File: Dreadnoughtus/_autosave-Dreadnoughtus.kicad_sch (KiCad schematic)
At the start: 403 parts

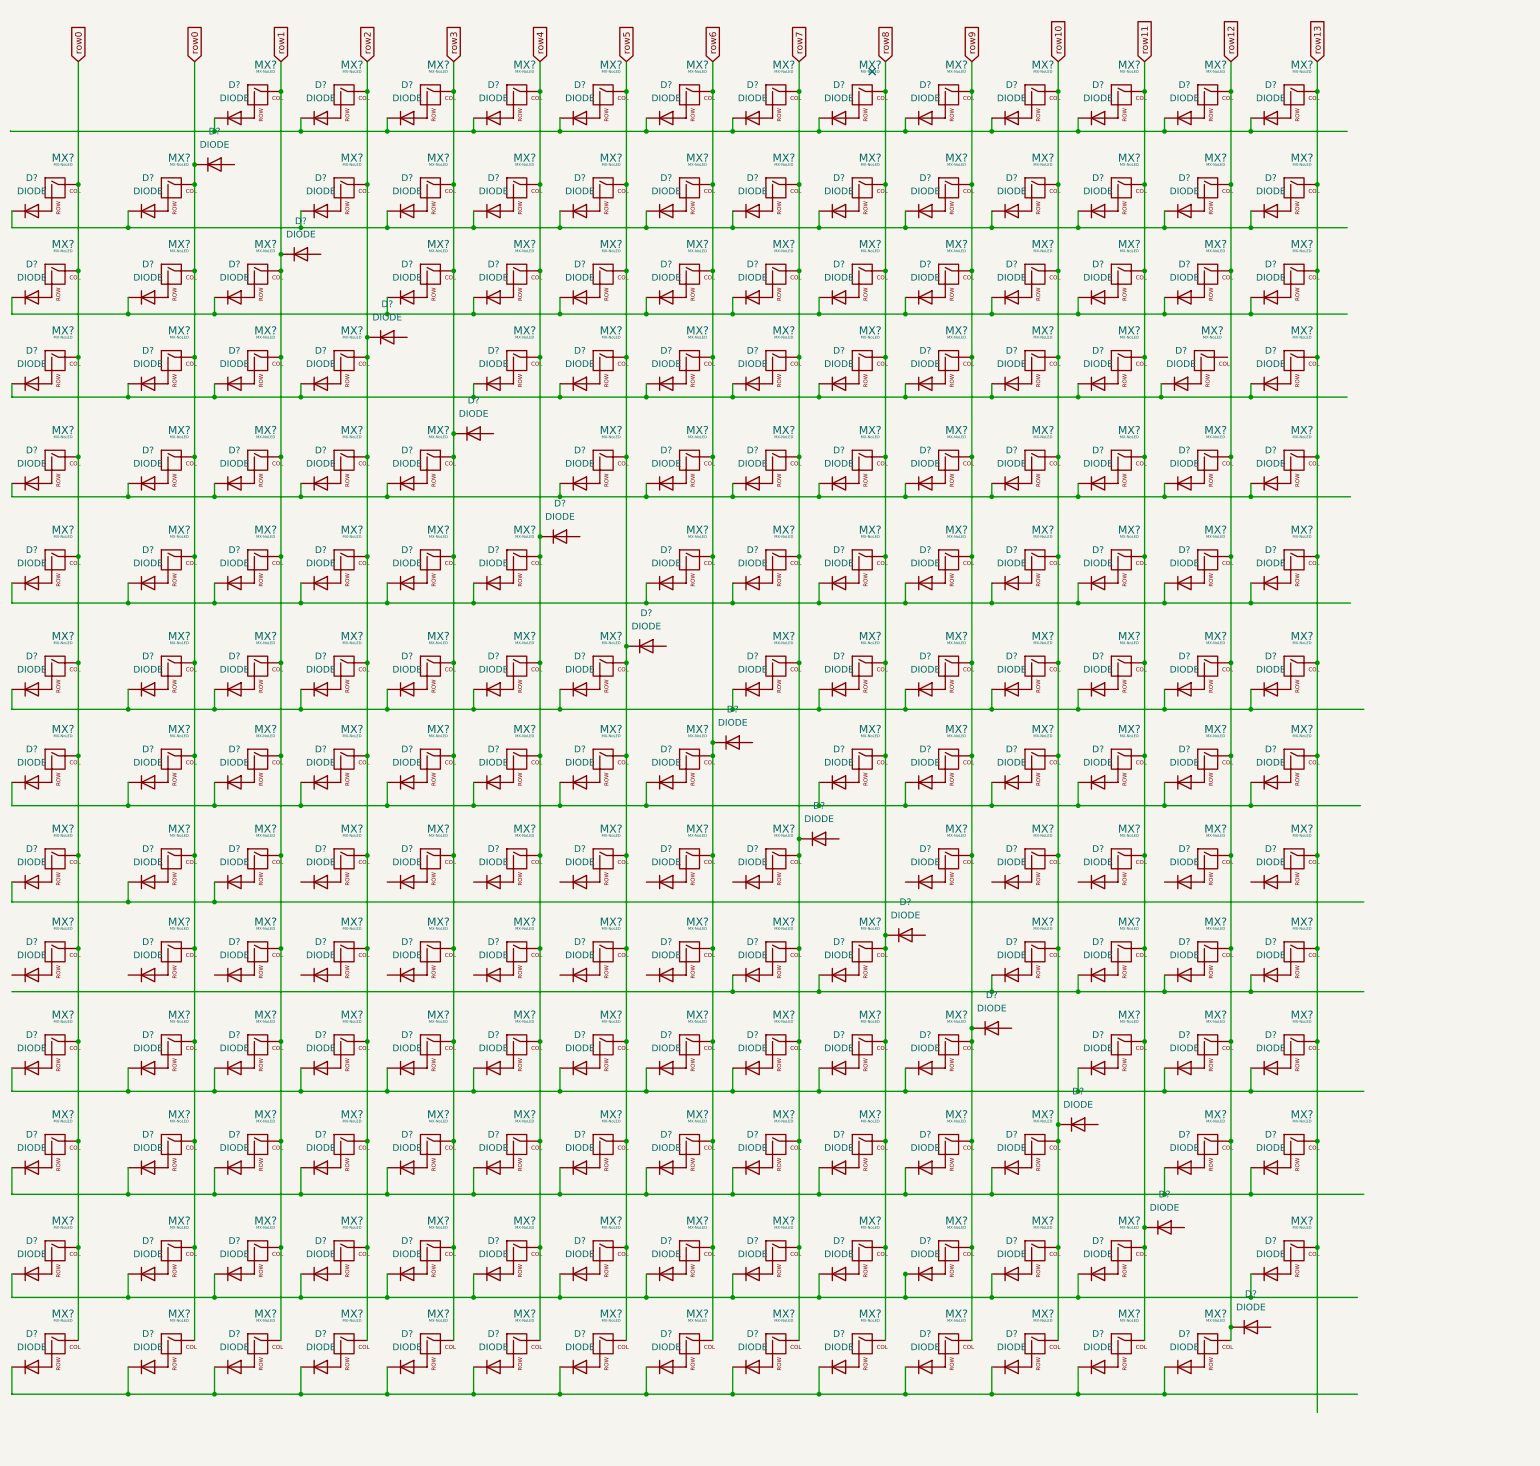
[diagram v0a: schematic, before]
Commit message: added keebio components
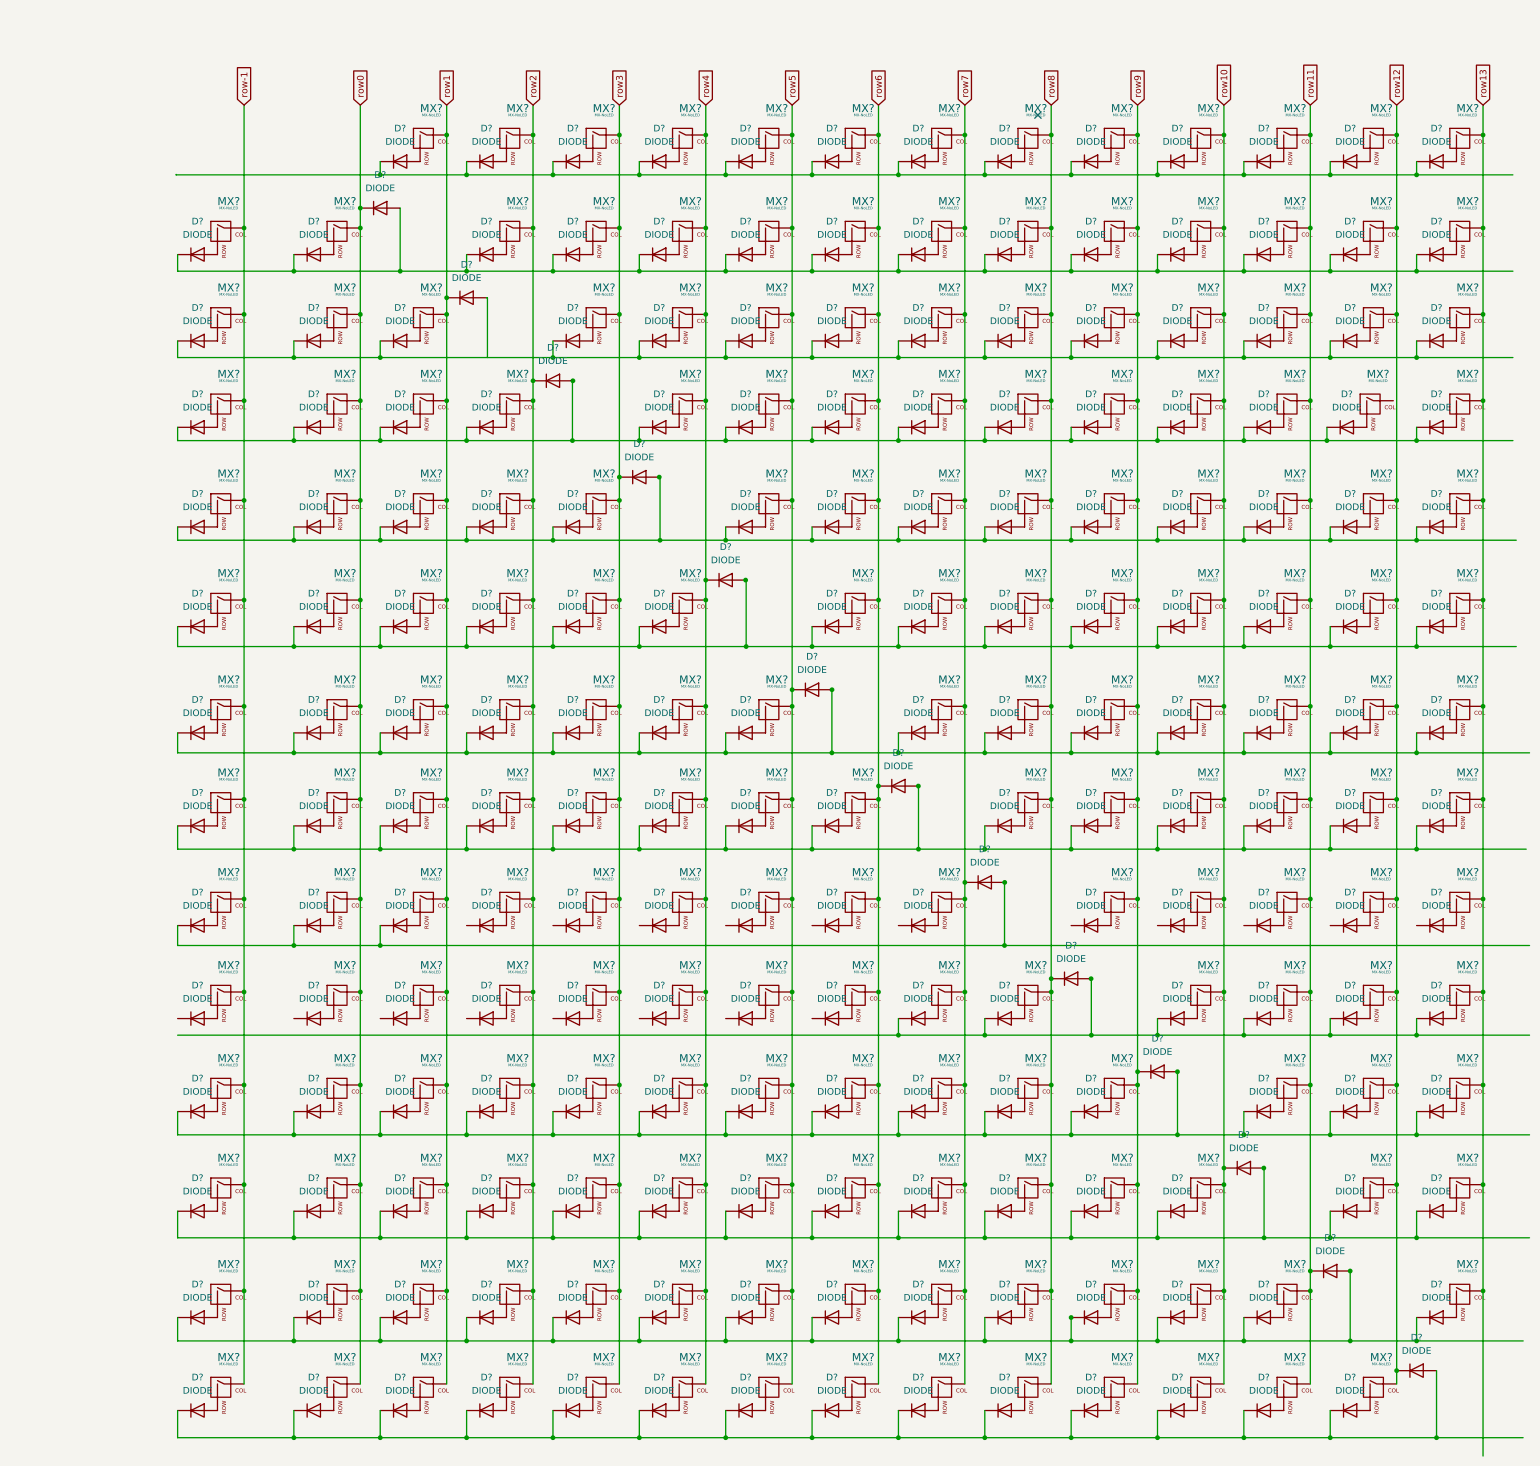
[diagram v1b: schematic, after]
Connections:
- net row0: no longer MX?.1 (COL), MX?.1 (COL), MX?.1 (COL), MX?.1 (COL), MX?.1 (COL), MX?.1 (COL), MX?.1 (COL), MX?.1 (COL), MX?.1 (COL), MX?.1 (COL), MX?.1 (COL), MX?.1 (COL), MX?.1 (COL)
- net at D?.2 (K), D?.2 (K), D?.2 (K)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: now also D?.1 (A) (x10)
- net at D?.2 (K), D?.2 (K), D?.2 (K): now also D?.1 (A)
- net at D?.2 (K), D?.2 (K), D?.2 (K)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: now also D?.1 (A)
- new net row-1: MX?.1 (COL), MX?.1 (COL), MX?.1 (COL), MX?.1 (COL), MX?.1 (COL), MX?.1 (COL), MX?.1 (COL), MX?.1 (COL), MX?.1 (COL), MX?.1 (COL), MX?.1 (COL), MX?.1 (COL), MX?.1 (COL)
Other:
- moved on the sheet: D?, MX?

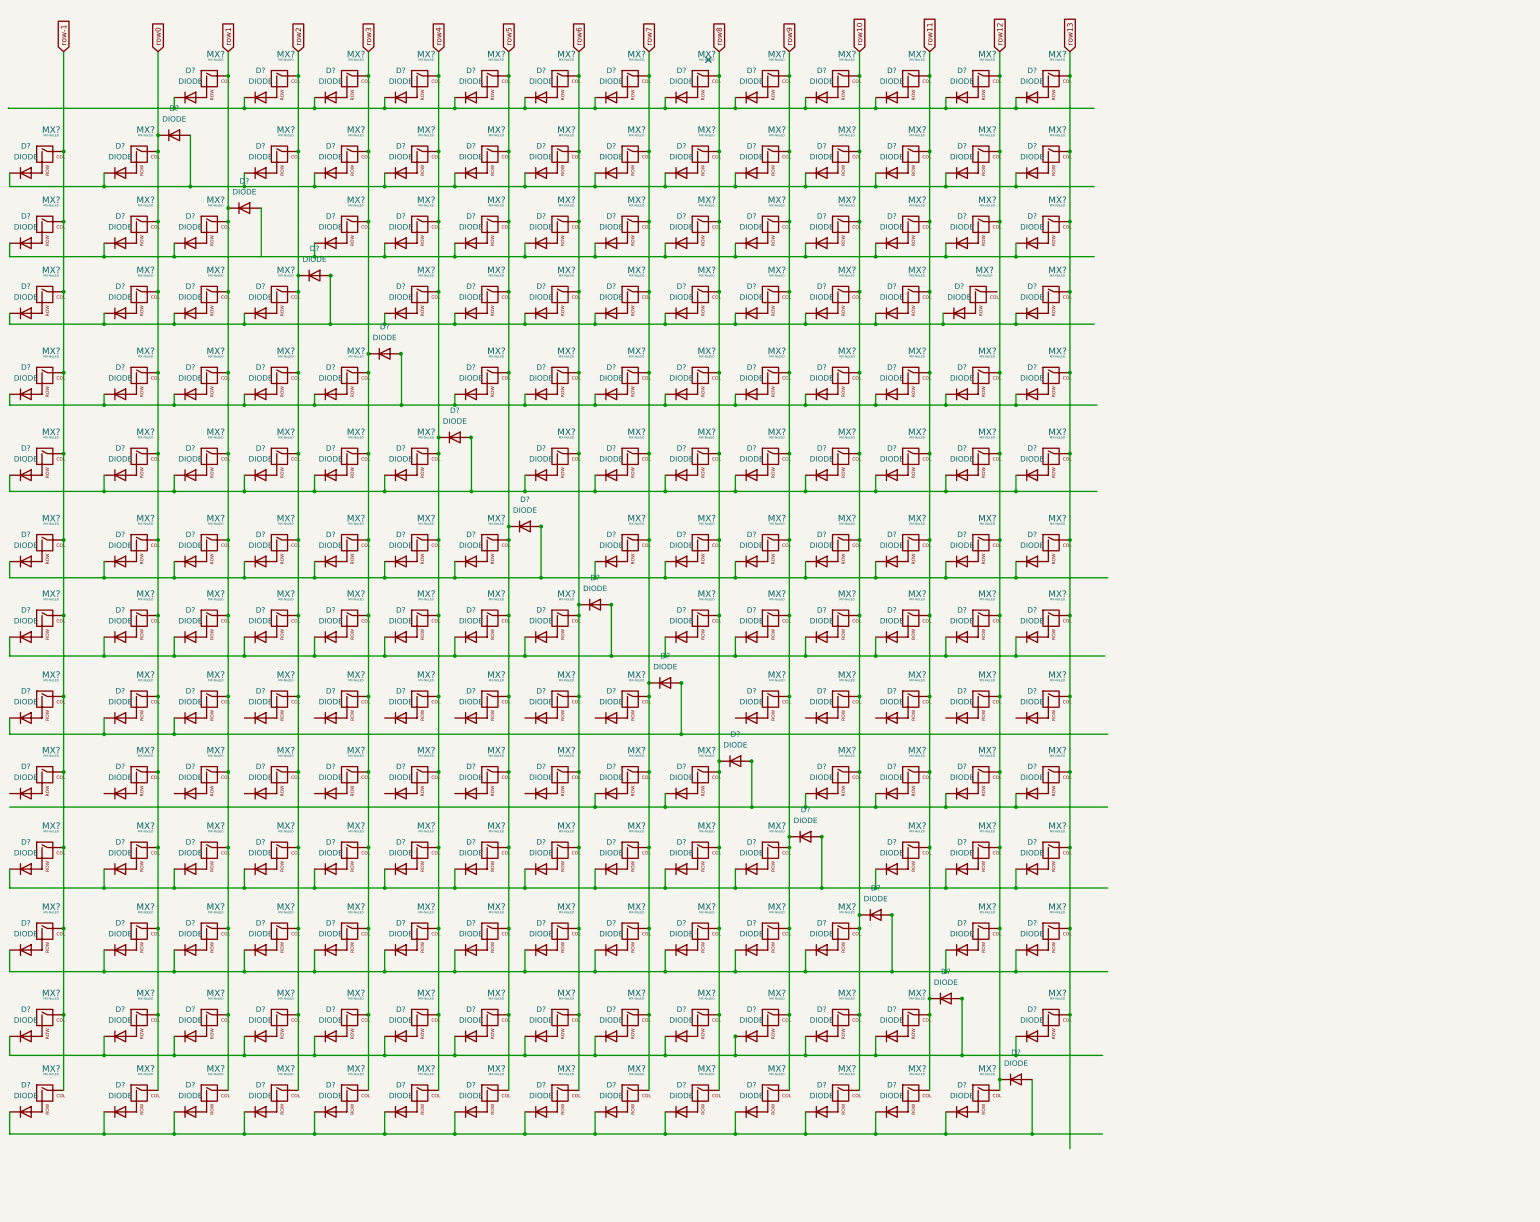
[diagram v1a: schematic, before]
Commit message: finalized matrix connections
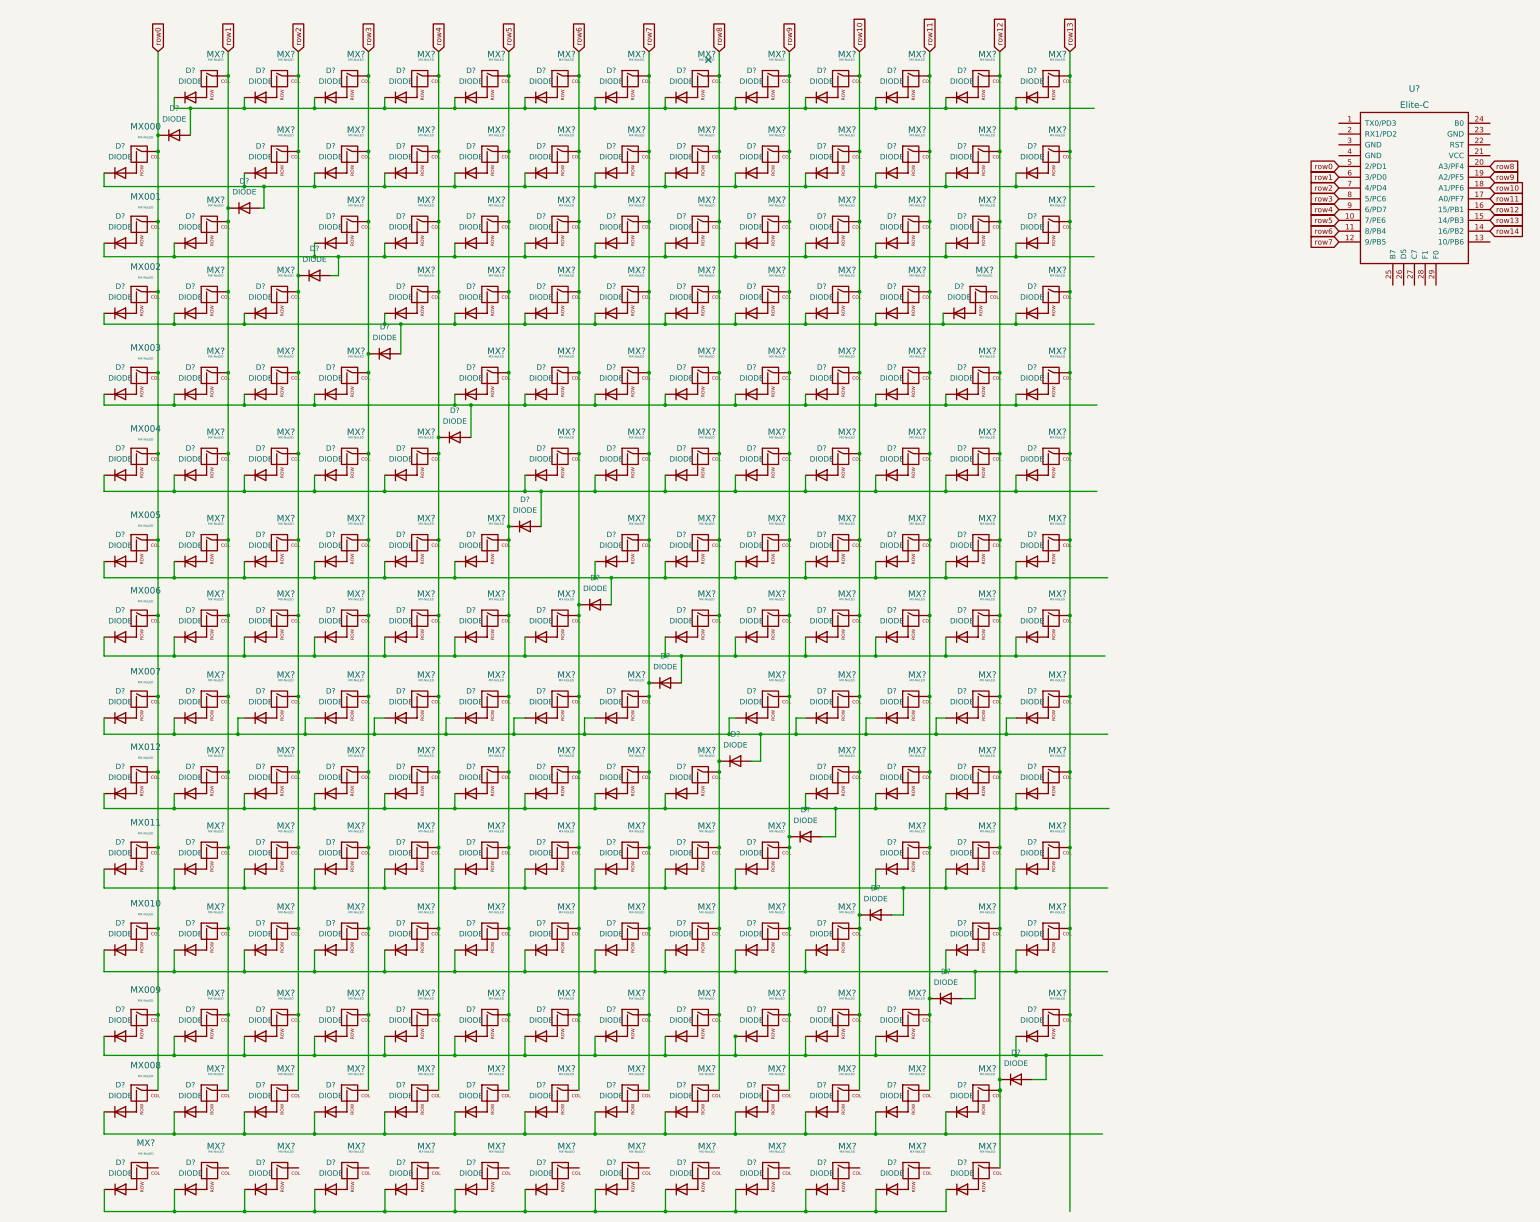
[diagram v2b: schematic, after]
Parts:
- removed D? (x13): DIODE, symbol Simulation_SPICE:DIODE
- removed MX? (x13): MX-NoLED, symbol MX_Alps_Hybrid:MX-NoLED
- added D? (x13): DIODE, symbol Simulation_SPICE:DIODE
- added MX? (x13): MX-NoLED, symbol MX_Alps_Hybrid:MX-NoLED
- added U?: Elite-C, symbol keebio:Elite-C
- gave numbers to parts that had none: 13
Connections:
- net row0: now also U?.5 (2/PD1)
- net row1: now also U?.6 (3/PD0)
- net row10: now also U?.18 (A1/PF6)
- net row11: now also U?.17 (A0/PF7)
- net row12: now also MX?.1 (COL), U?.16 (15/PB1)
- net row13: now also U?.15 (14/PB3)
- net row2: now also U?.7 (4/PD4)
- net row3: now also U?.8 (5/PC6)
- net row4: now also U?.9 (6/PD7)
- net row5: now also U?.10 (7/PE6)
- net row6: now also U?.11 (8/PB4)
- net row7: now also U?.12 (9/PB5)
- net row8: now also U?.20 (A3/PF4)
- net row9: now also U?.19 (A2/PF5)
- net at D?.2 (K), D?.2 (K), D?.2 (K)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: now also D?.1 (A); no longer D?.1 (A) (x9)
- net at D?.2 (K), D?.2 (K): now also D?.1 (A), D?.2 (K), D?.2 (K), D?.2 (K), D?.2 (K), D?.2 (K), D?.2 (K), D?.2 (K), D?.2 (K), D?.2 (K), D?.2 (K), D?.2 (K); no longer D?.1 (A)
- net at D?.2 (K), D?.2 (K), D?.2 (K)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: now also D?.1 (A) (x2)
- net at D?.2 (K), D?.2 (K), D?.2 (K)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: now also D?.1 (A), D?.2 (K), D?.2 (K), D?.2 (K), D?.2 (K), D?.2 (K), D?.2 (K), D?.2 (K); no longer D?.1 (A)
- net at D?.2 (K), D?.2 (K), D?.2 (K)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: no longer D?.1 (A)
- new net: D?.1 (A), MX?.2 (ROW) (x13)
- new net: D?.2 (K), D?.2 (K), D?.2 (K), D?.2 (K), D?.2 (K), D?.2 (K), D?.2 (K), D?.2 (K), D?.2 (K), D?.2 (K), D?.2 (K), D?.2 (K), D?.2 (K)
- new net row14: U?.14 (16/PB2)
